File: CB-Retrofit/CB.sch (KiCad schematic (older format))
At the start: 6 parts, among them J1 SD_Card, U1 LM386, U2 Teensy3.2

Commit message: WIP
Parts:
- removed J1: SD_Card, 10067847-001, symbol SD_Card
- added C2: 1µF, Capacitors_THT:C_Disc_D6.0mm_W2.5mm_P5.00mm, symbol C_Small
- added C4: C_Small, Capacitors_THT:C_Disc_D6.0mm_W2.5mm_P5.00mm, symbol C_Small
- added D1: LED, Pin_Headers:Pin_Header_Straight_1x02, symbol LED
- added R1, R2: 1k, Resistors_THT:Resistor_Vertical_RM5mm, symbol R
- added R3: R_Small, Resistors_THT:Resistor_Vertical_RM5mm, symbol R_Small
- added RV1: 10k LIN, Pin_Headers:Pin_Header_Straight_1x03, symbol POT
- added RV2: 10k AUDIO, Pin_Headers:Pin_Header_Straight_1x03, symbol POT
- added S1: 4PDT, 4pdt:4pdt, symbol 4PDT
- added SW1: SW_SPST, Connectors_JST:JST_EH_B02B-EH-A_02x2.50mm_Straight, symbol SW_SPST
- added SW2: 3pdt, 4pdt:3pdt, symbol 3pdt-RESCUE-CB
- added SW3: SW_Push, Connectors_JST:JST_EH_B02B-EH-A_02x2.50mm_Straight, symbol SW_Push
- added U1: PBOOST500, Pin_Headers:Pin_Header_Straight_1x08, symbol PBOOST500-RESCUE-CB-RESCUE-CB
- added U2: SD_Card_Module, Pin_Headers:Pin_Header_Straight_1x08, symbol SD_Card_Module
- added U4: AUDIOB_I2S, 4pdt:AudioB_I2S, symbol AUDIOB_I2S
- added U5: TDA1543, Housings_DIP:DIP-8_W7.62mm, symbol TDA1543
- C1: footprint (none) -> Capacitors_THT:C_Disc_D6.0mm_W2.5mm_P5.00mm
- C3: renamed from C2; footprint (none) -> Capacitors_THT:C_Disc_D6.0mm_W2.5mm_P5.00mm
- LS1: footprint (none) -> Connectors_JST:JST_EH_B02B-EH-A_02x2.50mm_Straight
- U3: renamed from U2; footprint (none) -> Teensy:Teensy30_31_32_LC
- U6: renamed from U1; footprint (none) -> Housings_DIP:DIP-8_W7.62mm
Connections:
- net labels added: BT_POW, CS, DI, DO, GNDA, LINE_OUT, SCK, TEENSY_POW, VCC
- wire segments 6 -> 75
- no-connect marks 0 -> 73
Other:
- note added: "Batt Test LED & Sw."
- note added: "Channel Switch"
- note added: "Mod LED"
- note added: "PTT Switch"
- note added: "Squelch Knob"
- note added: "Volume Knob"
- moved on the sheet: C1, C3, LS1, U6

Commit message: Cleaning up this rescue file bs
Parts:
- removed SW2: 3pdt, 4pdt:3pdt, symbol 3pdt-RESCUE-CB
- removed U1: PBOOST500, Pin_Headers:Pin_Header_Straight_1x08, symbol PBOOST500-RESCUE-CB-RESCUE-CB
- added SW?: 3pdt, symbol 3pdt
- added U?: PBOOST500, symbol PBOOST500
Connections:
- net +5V: now also SW?.3 (Cen1)
- net BT_POW: now also SW?.2 (P1-2)
- net GND: now also SW?.8 (Cen2), U?.2 (GND), U?.5 (GND), U?.7 (GND)
- net TEENSY_POW: now also SW?.1 (P1-1)
- net VCC: now also U?.1 (5Vin)
- net at U3.5 (3_TX_PWM): now also SW?.6 (P2-1)
- net at U3.6 (4_RX_PWM): now also SW?.7 (P2-2)
- net at U3.7 (5_TX1_PWM): now also SW?.9 (P2-3)
- net at SW1.2 (B), SW3.2: now also U?.8 (5Vout)
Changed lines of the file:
@@
 EESchema Schematic File Version 2
-LIBS:CB-rescue
 LIBS:power
 LIBS:device
@@
 $EndComp
 $Comp
-L 3pdt-RESCUE-CB SW2
-U 1 1 5A0E409A
-P 2300 1850
-F 0 "SW2" H 2300 1750 60  0000 C CNN
-F 1 "3pdt" H 2300 1900 60  0000 C CNN
-F 2 "4pdt:3pdt" H 2300 1650 60  0001 C CNN
-F 3 "" H 2300 1650 60  0001 C CNN
-	1    2300 1850
-	0    1    1    0
-$EndComp
-$Comp
 L GND #PWR06
 U 1 1 5A0E41E3
@@
 $EndComp
 $Comp
-L PBOOST500-RESCUE-CB-RESCUE-CB U1
-U 1 1 5A1AD8D2
-P 9800 1050
-F 0 "U1" H 9800 1050 60  0000 C CNN
-F 1 "PBOOST500" H 9800 950 60  0000 C CNN
-F 2 "Pin_Headers:Pin_Header_Straight_1x08" H 9800 1050 60  0001 C CNN
-F 3 "" H 9800 1050 60  0001 C CNN
-	1    9800 1050
-	1    0    0    -1
-$EndComp
-$Comp
 L VCC #PWR020
 U 1 1 5A1AD9C6
@@
 Text Label 7450 3050 2    60   ~ 0
 TEENSY_POW
+$Comp
+L 3pdt SW?
+U 1 1 5A1B8D26
+P 2300 1850
+F 0 "SW?" H 2300 1750 60  0000 C CNN
+F 1 "3pdt" H 2300 1900 60  0000 C CNN
+F 2 "" H 2300 1650 60  0001 C CNN
+F 3 "" H 2300 1650 60  0001 C CNN
+	1    2300 1850
+	0    1    1    0
+$EndComp
+$Comp
+L PBOOST500 U?
+U 1 1 5A1B8DA7
+P 9800 1050
+F 0 "U?" H 9800 1050 60  0000 C CNN
+F 1 "PBOOST500" H 9800 950 60  0000 C CNN
+F 2 "" H 9800 1050 60  0001 C CNN
+F 3 "" H 9800 1050 60  0001 C CNN
+	1    9800 1050
+	1    0    0    -1
+$EndComp
 $EndSCHEMATC

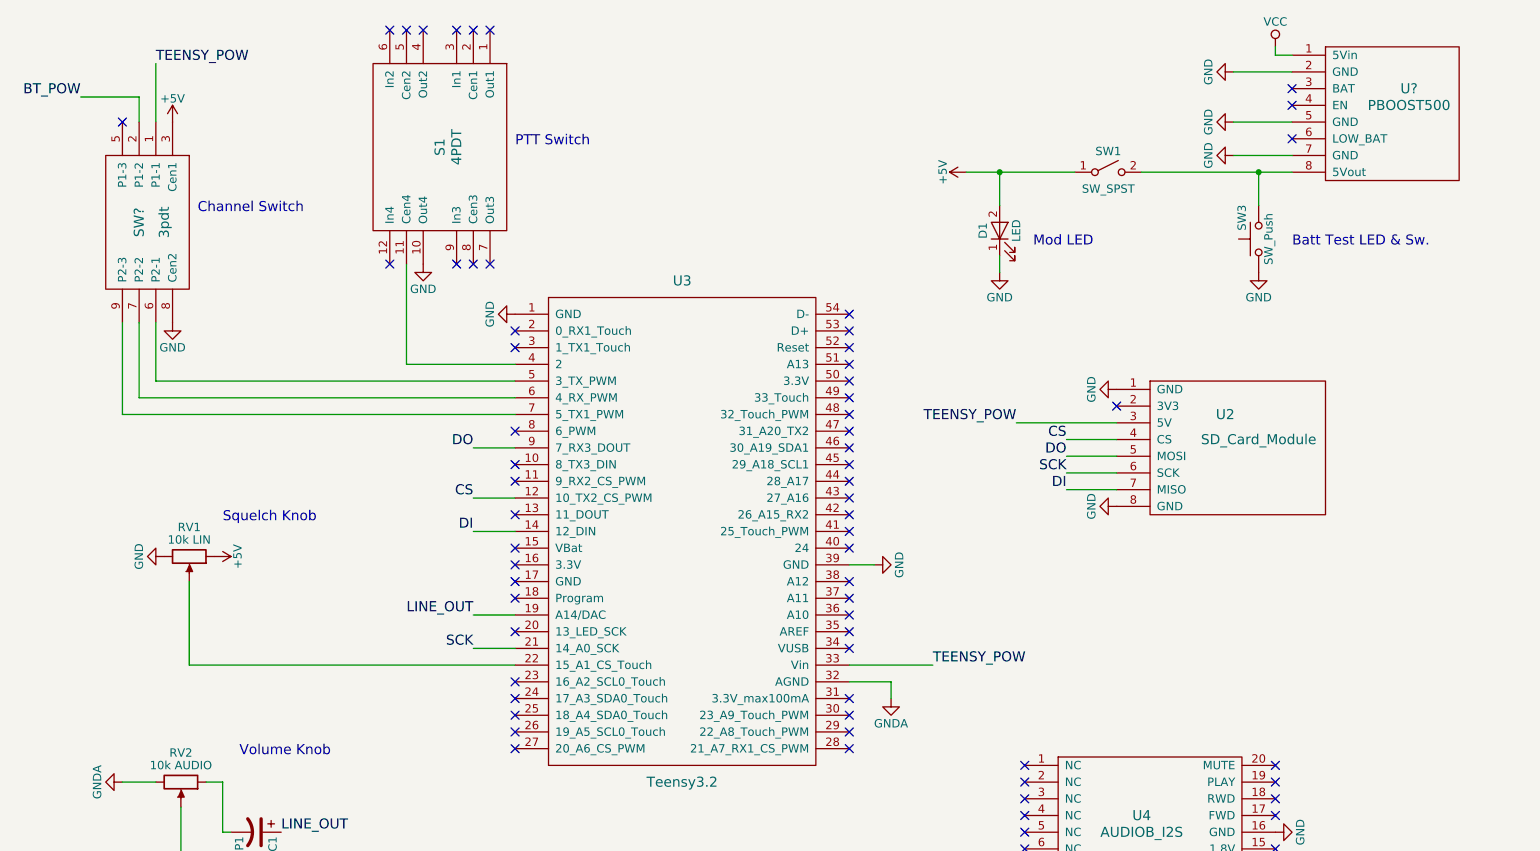
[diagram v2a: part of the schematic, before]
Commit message: First possible PCB, needs a few more footprints
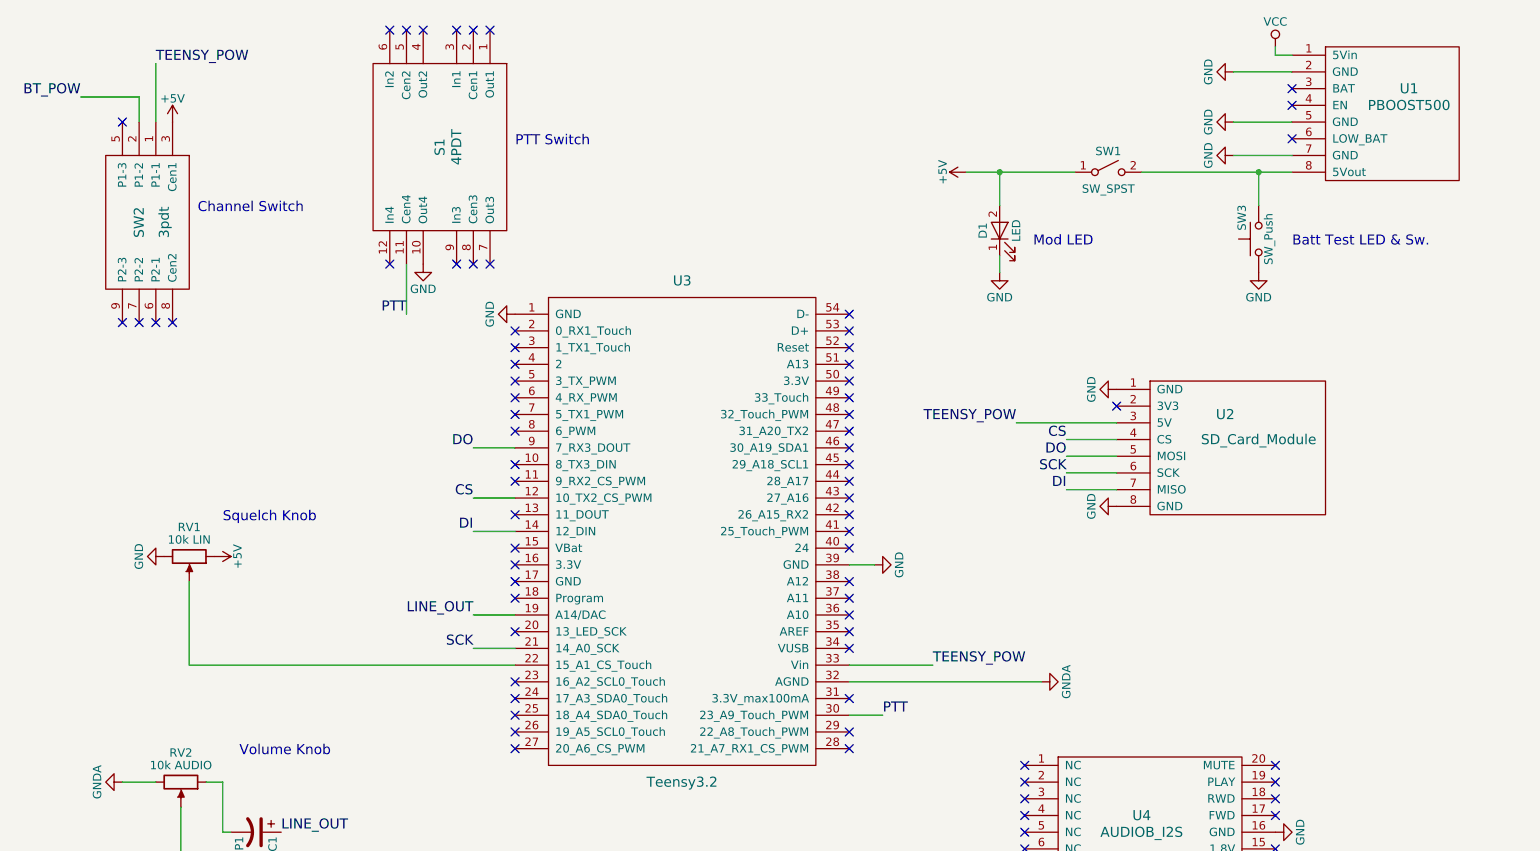
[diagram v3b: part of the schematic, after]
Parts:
- removed U?: PBOOST500, symbol PBOOST500
- added U1: PBOOST500, symbol PBOOST500
- gave numbers to parts that had none: 1
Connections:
- net GND: now also U1.2 (GND), U1.5 (GND), U1.7 (GND); no longer SW2.8 (Cen2)
- net VCC: now also U1.1 (5Vin)
- net PTT: now reaches U3.30 (23_A9_Touch_PWM)
- net PTT: now also S1.11 (Cen4)
- net at U3.4 (2): no longer S1.11 (Cen4)
- net at U3.5 (3_TX_PWM): no longer SW2.6 (P2-1)
- net at U3.6 (4_RX_PWM): no longer SW2.7 (P2-2)
- net at U3.7 (5_TX1_PWM): no longer SW2.9 (P2-3)
- net at SW1.2 (B), SW3.2: now also U1.8 (5Vout)
- no-connect marks 73 -> 80
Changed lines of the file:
@@
 EESchema Schematic File Version 2
-LIBS:power
-LIBS:device
-LIBS:transistors
-LIBS:conn
-LIBS:linear
-LIBS:regul
-LIBS:74xx
-LIBS:cmos4000
-LIBS:adc-dac
-LIBS:memory
-LIBS:xilinx
-LIBS:microcontrollers
-LIBS:dsp
-LIBS:microchip
-LIBS:analog_switches
-LIBS:motorola
-LIBS:texas
-LIBS:intel
-LIBS:audio
-LIBS:interface
-LIBS:digital-audio
-LIBS:philips
-LIBS:display
-LIBS:cypress
-LIBS:siliconi
-LIBS:opto
-LIBS:atmel
-LIBS:contrib
-LIBS:valves
-LIBS:teensy
 LIBS:4pdt
-LIBS:switches
 LIBS:CB-cache
 EELAYER 25 0
@@
 F 3 "" H 3900 2100 50  0001 C CNN
 	1    3900 2100
-	1    0    0    -1
-$EndComp
-$Comp
-L GND #PWR06
-U 1 1 5A0E41E3
-P 2400 2450
-F 0 "#PWR06" H 2400 2200 50  0001 C CNN
-F 1 "GND" H 2400 2300 50  0000 C CNN
-F 2 "" H 2400 2450 50  0001 C CNN
-F 3 "" H 2400 2450 50  0001 C CNN
-	1    2400 2450
 	1    0    0    -1
 $EndComp
@@
 	4200 4200 4450 4200
 Wire Wire Line
-	3800 2100 3800 2700
-Wire Wire Line
-	3800 2700 4450 2700
-Wire Wire Line
-	4450 2800 2300 2800
-Wire Wire Line
-	2300 2800 2300 2450
-Wire Wire Line
-	4450 2900 2200 2900
-Wire Wire Line
-	2200 2900 2200 2450
-Wire Wire Line
-	4450 3000 2100 3000
-Wire Wire Line
-	2100 3000 2100 2450
-Wire Wire Line
 	8050 3450 7750 3450
 Wire Wire Line
@@
 L GNDA #PWR010
 U 1 1 5A1A38AF
-P 6700 4700
-F 0 "#PWR010" H 6700 4450 50  0001 C CNN
-F 1 "GNDA" H 6700 4550 50  0000 C CNN
-F 2 "" H 6700 4700 50  0001 C CNN
-F 3 "" H 6700 4700 50  0001 C CNN
-	1    6700 4700
-	1    0    0    -1
-$EndComp
-Wire Wire Line
-	6450 4600 6700 4600
+P 7600 4600
+F 0 "#PWR010" H 7600 4350 50  0001 C CNN
+F 1 "GNDA" H 7600 4450 50  0000 C CNN
+F 2 "" H 7600 4600 50  0001 C CNN
+F 3 "" H 7600 4600 50  0001 C CNN
+	1    7600 4600
+	0    -1   -1   0
+$EndComp
+Wire Wire Line
+	6450 4600 7600 4600
 $Comp
 L +5V #PWR011
@@
 NoConn ~ 6450 4400
 NoConn ~ 6450 4700
-NoConn ~ 6450 4800
 NoConn ~ 6450 4900
 NoConn ~ 6450 5000
@@
 Wire Wire Line
 	6950 4500 6450 4500
-Wire Wire Line
-	6700 4600 6700 4700
 $Comp
 L GND #PWR027
@@
 TEENSY_POW
 $Comp
-L 3pdt SW?
+L 3pdt SW2
 U 1 1 5A1B8D26
 P 2300 1850
-F 0 "SW?" H 2300 1750 60  0000 C CNN
+F 0 "SW2" H 2300 1750 60  0000 C CNN
 F 1 "3pdt" H 2300 1900 60  0000 C CNN
 F 2 "" H 2300 1650 60  0001 C CNN
@@
 $EndComp
 $Comp
-L PBOOST500 U?
-U 1 1 5A1B8DA7
+L PBOOST500 U1
+U 1 1 5A1B34A1
 P 9800 1050
-F 0 "U?" H 9800 1050 60  0000 C CNN
+F 0 "U1" H 9800 1050 60  0000 C CNN
 F 1 "PBOOST500" H 9800 950 60  0000 C CNN
 F 2 "" H 9800 1050 60  0001 C CNN
@@
 	1    0    0    -1
 $EndComp
+Wire Wire Line
+	3800 2100 3800 2400
+Text Label 3800 2400 2    60   ~ 0
+PTT
+Text Label 6650 4800 0    60   ~ 0
+PTT
+Wire Wire Line
+	6650 4800 6450 4800
+NoConn ~ 4450 2700
+NoConn ~ 2100 2450
+NoConn ~ 2200 2450
+NoConn ~ 2300 2450
+NoConn ~ 2400 2450
+NoConn ~ 4450 3000
+NoConn ~ 4450 2900
+NoConn ~ 4450 2800
 $EndSCHEMATC

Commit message: Second attempt
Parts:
- added J1: PowerJack, 4pdt:Power_Jack, symbol PowerJack
- added J2: POT_MOUNT, 4pdt:POT_MOUNT, symbol POT_MOUNT
- added SW1: SW_SPST, Connectors_JST:JST_EH_B02B-EH-A_02x2.50mm_Straight, symbol SW_SPST
- SW3: renamed from SW2; footprint (none) -> 4pdt:3pdt
- U1: footprint (none) -> Pin_Headers:Pin_Header_Straight_1x08
- renumbered SW1 to SW2, SW3 to SW4
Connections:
- net GND: now also J1.8 (Power-), J2.1 (GND), J2.2 (GND)
- net VCC: now also J1.7 (Power+)
- no-connect marks 80 -> 87
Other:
- note added: "Hi-Lo Switch"
- moved on the sheet: D1, SW2, SW4, U1
